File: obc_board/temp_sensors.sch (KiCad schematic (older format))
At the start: 84 parts, among them U10 BMM150, U4 LTC4304CMSTRPBF, U5 MCP9600-E_MX, U6 MCP9600-E_MX, U7 MCP9600-E_MX, U8 MCP9600-E_MX, U9 BMI160

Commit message: modify planes
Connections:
- net CSB renamed CSB_GYRO
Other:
- moved on the sheet: C29, C30, C31, C32, R44, R46, U10, U9

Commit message: add imu and mux
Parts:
- removed C22, C24, C25, C26, C27, C28: 100n, Capacitor_SMD:C_0402_1005Metric, symbol Device:C
- removed D10, D11, D12, D13, D14, D15, D16, D2, D4, D7, D8, D9: BAT48RL, Diode_SMD:D_MiniMELF, symbol Diode:BAT48RL
- removed L3, L4, L5, L6, L7, L8: 300n, Inductor_SMD:L_1210_3225Metric, symbol Device:L
- removed R11, R14, R28, R29, R30, R31: 2M, Resistor_SMD:R_0603_1608Metric, symbol Device:R
- removed R18, R32, R35: 1M, Resistor_SMD:R_0603_1608Metric, symbol Device:R
- removed R19, R20, R33, R34, R36, R37: 100, Resistor_SMD:R_0402_1005Metric, symbol Device:R
- removed R22, R38, R40: 10k, Resistor_SMD:R_0402_1005Metric, symbol Device:R
- removed R23: 4.3k, Resistor_SMD:R_0402_1005Metric, symbol Device:R
- removed R39: 2.2k, Resistor_SMD:R_0402_1005Metric, symbol Device:R
- removed R41: 7.5k, Resistor_SMD:R_0402_1005Metric, symbol Device:R
- removed R42, R43, R45, R47: 0, Resistor_SMD:R_0402_1005Metric, symbol Device:R
- removed U6, U7, U8: MCP9600-E_MX, Package_DFN_QFN:QFN-20-1EP_5x5mm_P0.65mm_EP3.35x3.35mm_ThermalVias, symbol cubesat_obc_lib:MCP9600-E_MX
- added C?: 4.7u, symbol Device:C
- added C?: 22p, symbol Device:C
- added C?: 10u, symbol Device:C
- added L? (x2): 4.7u, symbol Device:L
- added R?: 330k, symbol Device:R
- added TEMP4, TEMP5: Conn_01x02_Female, Connector_Molex:Molex_PicoBlade_53261-0271_1x02-1MP_P1.25mm_Horizontal, symbol Connector:Conn_01x02_Female
- added U?: LT3483ES6, symbol cubesat_obc_lib:LT3483ES6
- added U?: ADG1607, symbol cubesat_obc_lib:ADG1607
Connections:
- net 3V3: now also C23.1, D3.1 (K), R15.1, U5.8 (VDD), C?.1, L?.1, U?.25 (VSS), U?.4 (SHDN), U?.6 (VIN)
- net 3V3_1: no longer C23.1, D3.1 (K), R15.1, U5.8 (VDD)
- net GND: now also C?.2, C?.2, U?.2 (GND), U?.9 (GND)
- net at TEMP0.1 (Pin_1): now also U?.24 (S8A); no longer L2.1
- net at TEMP0.2 (Pin_2): now also U?.1 (S8B); no longer L1.1
- net at TEMP1.1 (Pin_1): now also U?.23 (S7A)
- net at TEMP1.2 (Pin_2): now also U?.2 (S7B)
- net at TEMP2.1 (Pin_1): now also U?.22 (S6A)
- net at TEMP2.2 (Pin_2): now also U?.3 (S6B)
- net at TEMP3.1 (Pin_1): now also U?.21 (S5A)
- net at TEMP3.2 (Pin_2): now also U?.4 (S5B)
- new net: L1.1, U?.27 (DA)
- new net: L2.1, U?.31 (DB)
- new net: L?.2, U?.1 (SW)
- new net: C?.2, R?.2, U?.3 (FB)
- new net: L?.1, U?.5 (D)
- new net: TEMP5.1 (Pin_1), U?.19 (S3A)
- new net: TEMP4.1 (Pin_1), U?.20 (S4A)
- new net: C?.1, C?.1, L?.2, R?.1, U?.29 (VDD)
- new net: TEMP4.2 (Pin_2), U?.5 (S4B)
- new net: TEMP5.2 (Pin_2), U?.6 (S3B)
- new net MUL_A0: U?.15 (A0)
- new net MUL_A1: U?.14 (A1)
- new net MUL_A2: U?.10 (A2)
- new net MUL_EN: U?.16 (EN)
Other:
- moved on the sheet: C21, C23, C31, C32, D1, D3, D5, D6, L1, L2, R10, R13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

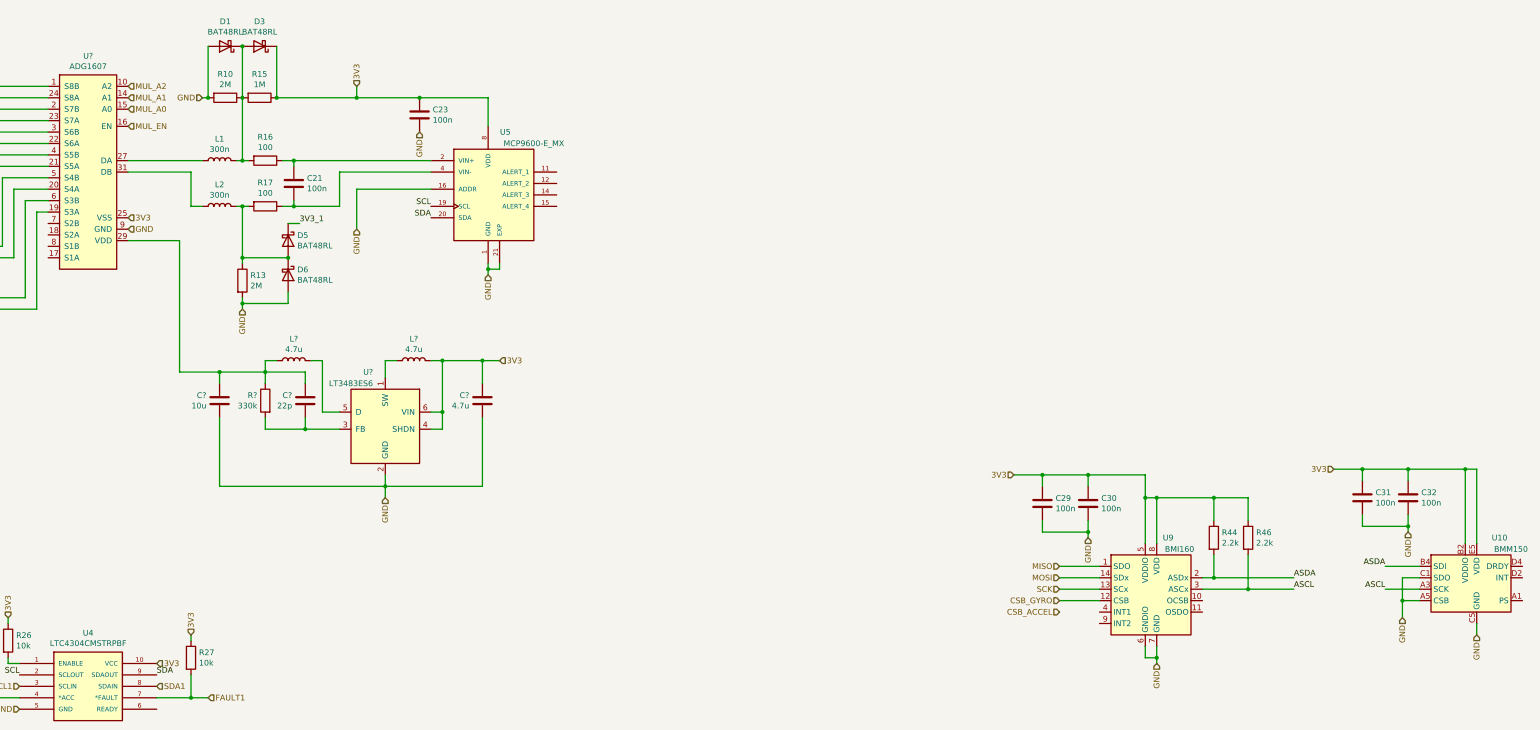
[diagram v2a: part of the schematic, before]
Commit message: added h bridge and magnetometers
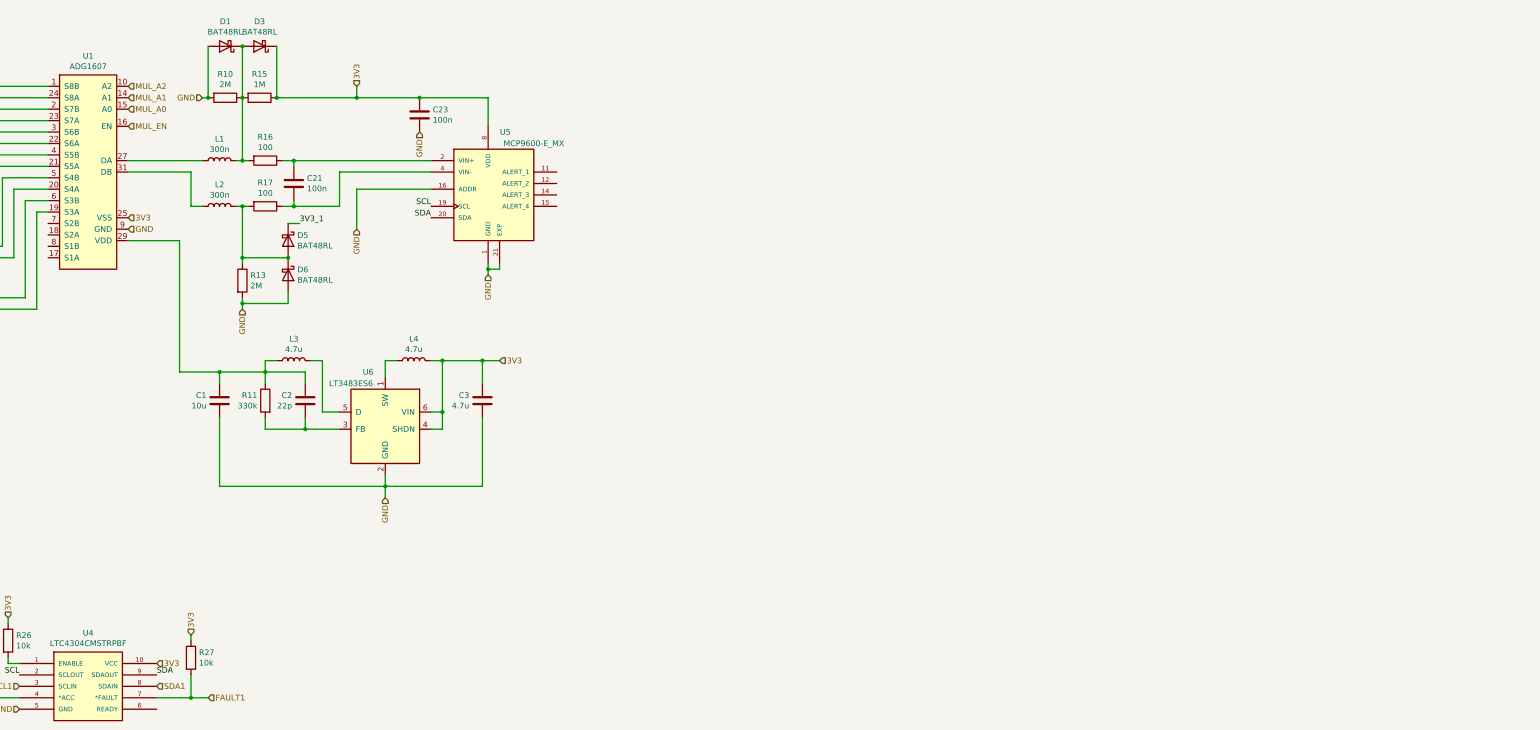
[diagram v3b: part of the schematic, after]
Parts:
- removed C29, C30, C31, C32: 100n, Capacitor_SMD:C_0402_1005Metric, symbol Device:C
- removed R44, R46: 2.2k, Resistor_SMD:R_0402_1005Metric, symbol Device:R
- removed U10: BMM150, Package_CSP:WLCSP-12_1.56x1.56mm_P0.4mm, symbol cubesat_obc_lib:BMM150
- removed U9: BMI160, Package_LGA:Bosch_LGA-14_3x2.5mm_P0.5mm, symbol cubesat_obc_lib:BMI160
- C1: renamed from C?; footprint (none) -> Capacitor_SMD:C_1206_3216Metric; Digikey Part Number (none) -> 311-1952-1-ND
- C2: renamed from C?; footprint (none) -> Capacitor_SMD:C_0402_1005Metric; Digikey Part Number (none) -> 311-1018-1-ND
- C3: renamed from C?; footprint (none) -> Capacitor_SMD:C_0805_2012Metric; Digikey Part Number (none) -> 490-9618-1-ND
- L3, L4: renamed from L?; footprint (none) -> cubesat_obc:L_Vishay_IHLP-2020; Digikey Part Number (none) -> 541-1222-1-ND
- R11: renamed from R?; footprint (none) -> Resistor_SMD:R_0402_1005Metric; Digikey Part Number (none) -> 311-330KLRCT-ND
- U1: renamed from U?; footprint (none) -> Package_CSP:LFCSP-32-1EP_5x5mm_P0.5mm_EP3.1x3.1mm; Digikey Part Number (none) -> ADG1607BCPZ-REEL7CT-ND
- U6: renamed from U?; footprint (none) -> Package_DFN_QFN:DFN-8-1EP_2x2mm_P0.45mm_EP0.64x1.38mm; Digikey Part Number (none) -> LT3483IDC#TRMPBFCT-ND

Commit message: reroute
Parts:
- U4: Field4 (none) -> Linear Technology
- U5: Field4 (none) -> Microchip; Field5 (none) -> 1.00mm; Field6 (none) -> IPC-7351B
- renumbered TEMP1 to TEMP0, TEMP0 to TEMP1
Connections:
- net at TEMP2.1 (Pin_1): now also U1.21 (S5A); no longer U1.22 (S6A)
- net at TEMP2.2 (Pin_2): now also U1.4 (S5B); no longer U1.3 (S6B)
- net at TEMP3.1 (Pin_1): now also U1.22 (S6A); no longer U1.21 (S5A)
- net at TEMP3.2 (Pin_2): now also U1.3 (S6B); no longer U1.4 (S5B)
- net at U1.19 (S3A): now also TEMP4.1 (Pin_1); no longer TEMP5.1 (Pin_1)
- net at U1.20 (S4A): now also TEMP5.1 (Pin_1); no longer TEMP4.1 (Pin_1)
- net at U1.5 (S4B): now also TEMP5.2 (Pin_2); no longer TEMP4.2 (Pin_2)
- net at U1.6 (S3B): now also TEMP4.2 (Pin_2); no longer TEMP5.2 (Pin_2)
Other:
- moved on the sheet: TEMP2, TEMP3, TEMP4, TEMP5
